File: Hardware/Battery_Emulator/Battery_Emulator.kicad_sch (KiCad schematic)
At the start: 15 parts, among them J1 Screw_Terminal_01x02, J2 USB4105-GF-A-060, U10 ATmega328PB-A, U3 74AHC2G125DP,125, U4 FT230XS-R, U5 LM7805_TO220, U9 ECS-160-7-33B2-CTN-TR3

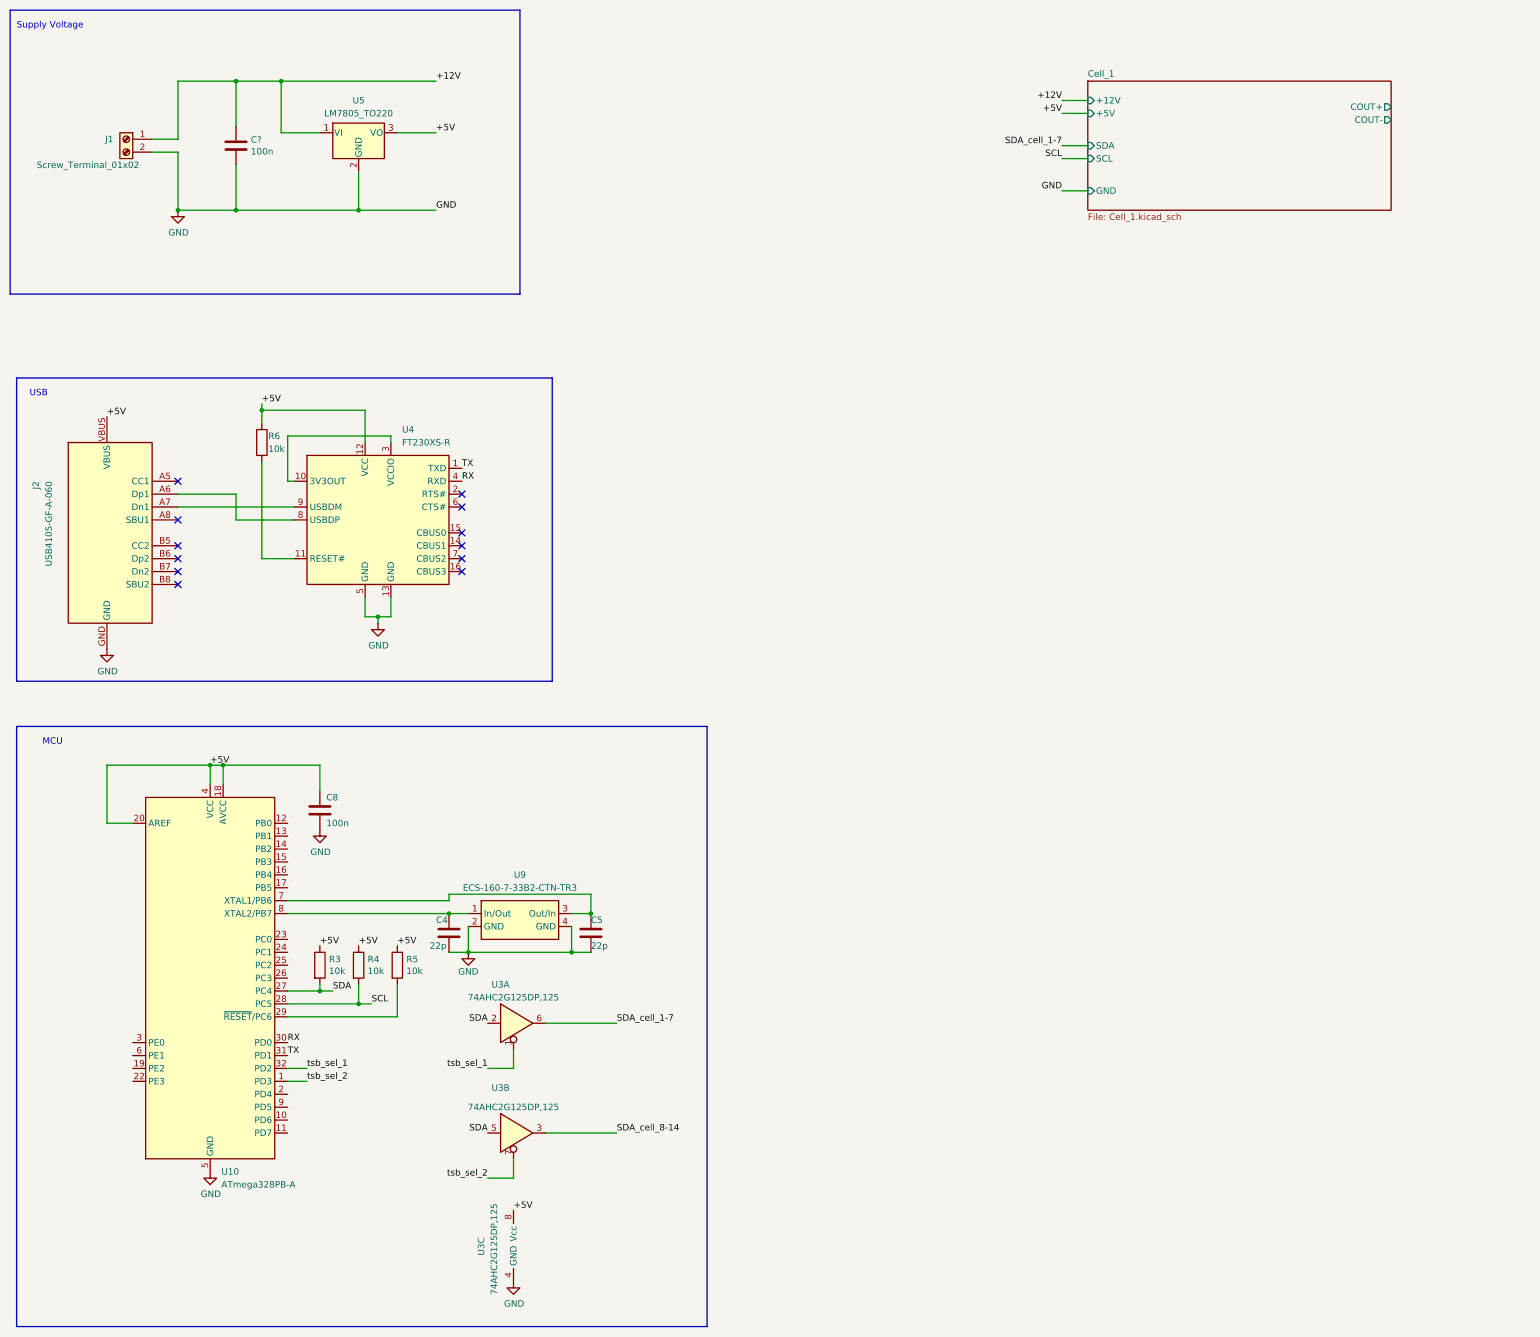
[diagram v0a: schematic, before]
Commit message: Updated schematic battery emulator
Made schematic more clear. Fixed some bugs
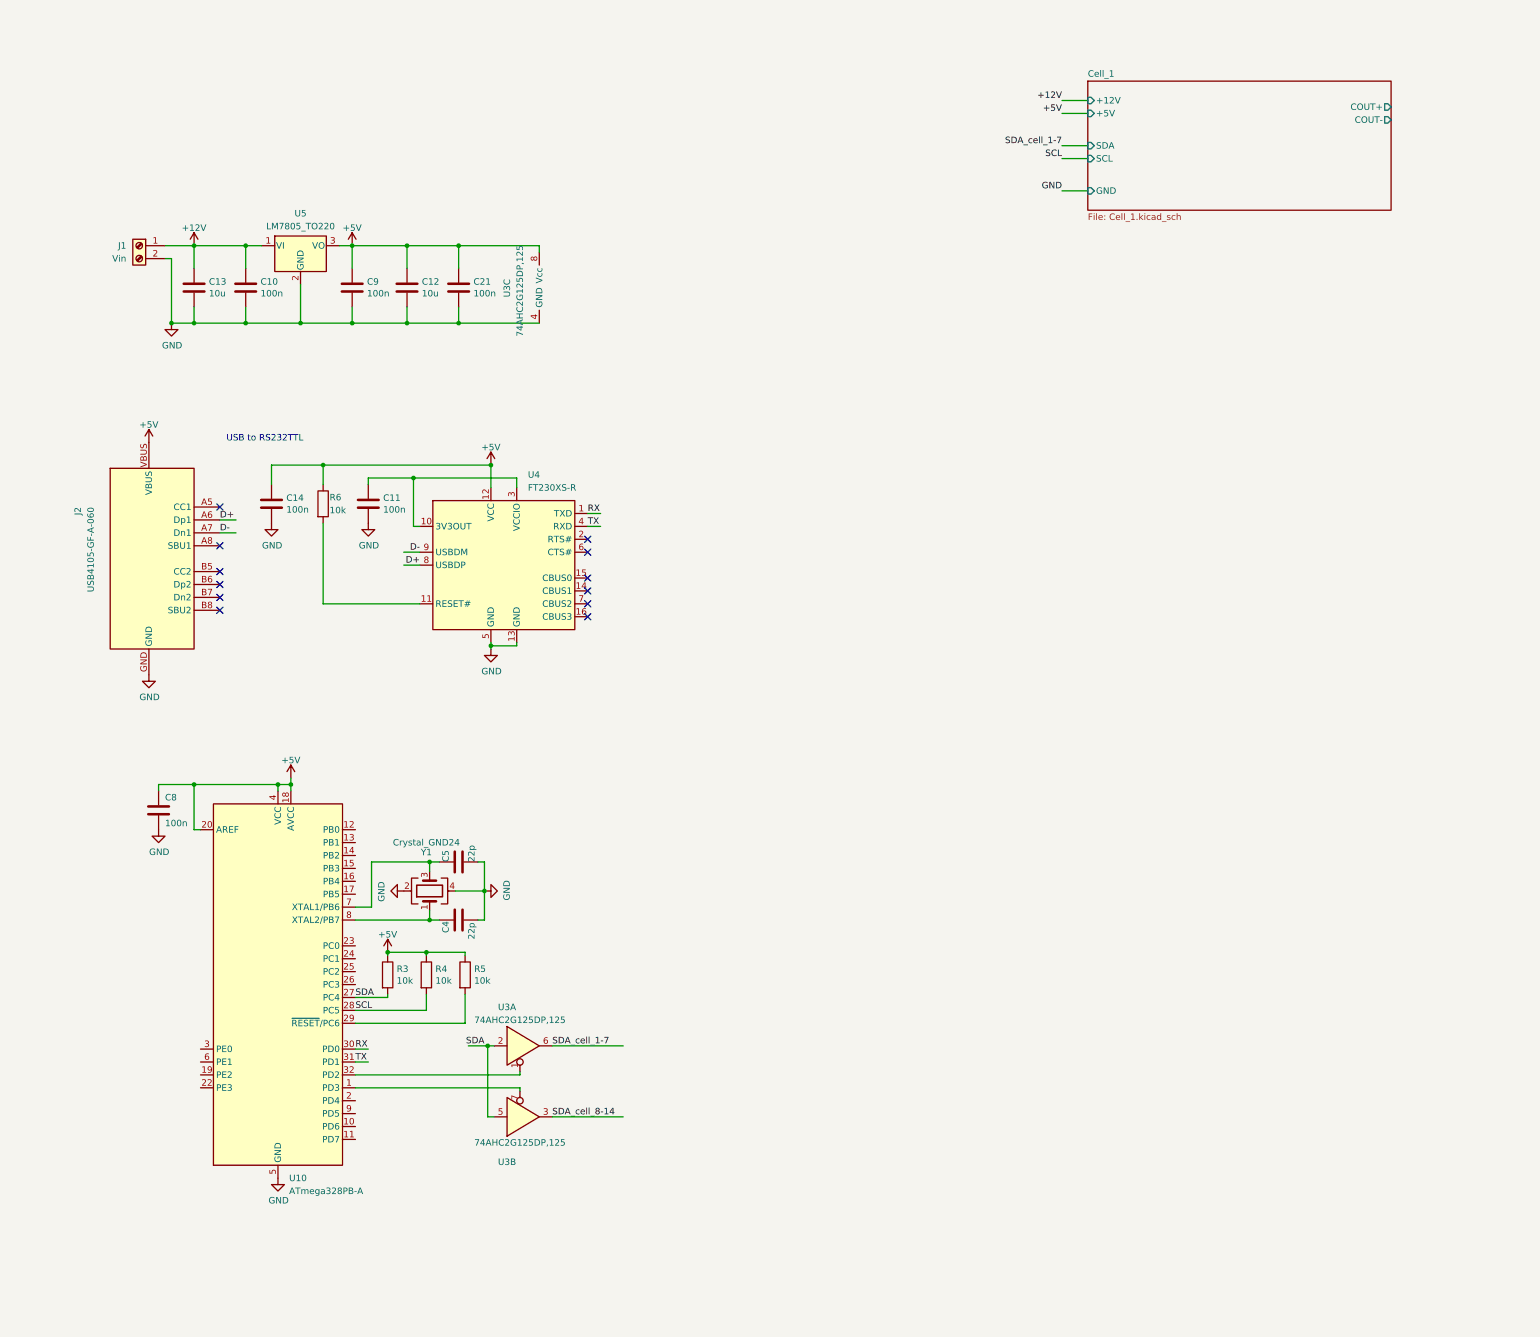
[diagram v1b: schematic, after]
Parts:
- removed U9: ECS-160-7-33B2-CTN-TR3, Crystal:Crystal_SMD_3225-4Pin_3.2x2.5mm, symbol PR7 Custom:ECS-160-7-33B2-CTN-TR3
- added C11, C14, C21, C9: 100n, Capacitor_SMD:C_0805_2012Metric, symbol Device:C
- added C12, C13: 10u, Capacitor_SMD:C_0805_2012Metric, symbol Device:C
- added Y1: Crystal_GND24, Crystal:Crystal_SMD_3225-4Pin_3.2x2.5mm, symbol Device:Crystal_GND24
- J1: value Screw_Terminal_01x02 -> Vin
- gave numbers to parts that had none: 1
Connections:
- net +12V: now also C13.1
- net +5V: now also C12.1, C14.1, C21.1, C9.1
- net GND: now also C11.2, C12.2, C13.2, C14.2, C21.2, C9.2, Y1.2, Y1.4
- net RX: now also U4.1 (TXD); no longer U4.4 (RXD)
- net TX: now also U4.4 (RXD); no longer U4.1 (TXD)
- net D+: now reaches J2.A6 (Dp1), U4.8 (USBDP)
- net D-: now reaches J2.A7 (Dn1), U4.9 (USBDM)
- net at C5.1, U10.7 (XTAL1/PB6): now also Y1.3
- net at C4.1, U10.8 (XTAL2/PB7): now also Y1.1
- net at U4.10 (3V3OUT), U4.3 (VCCIO): now also C11.1
- net tsb_sel_1: no longer names the net of U10.32 (PD2), U3.1
- net tsb_sel_2: no longer names the net of U10.1 (PD3), U3.7
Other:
- note added: "USB to RS232TTL"
- note removed: "MCU"
- note removed: "Supply Voltage"
- note removed: "USB"
- moved on the sheet: C10, C4, C5, C8, J1, J2, R3, R4, R5, R6, U10, U3A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

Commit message: Added components to PCB and started the layout
Also added footprints for the pots, jumpers and power connector
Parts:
- J1: footprint (none) -> Connector_PinSocket_2.00mm:PinSocket_1x02_P2.00mm_Vertical
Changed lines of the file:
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@@
       (effects (font (size 1.27 1.27)) (justify left))
     )
-    (property "Footprint" "" (at 39.37 60.325 0)
+    (property "Footprint" "Connector_PinSocket_2.00mm:PinSocket_1x02_P2.00mm_Vertical" (at 39.37 60.325 0)
       (effects (font (size 1.27 1.27)) hide)
     )

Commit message: Update PCB
Made PCB in Kicad
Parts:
- added C22: 100n, Capacitor_SMD:C_0805_2012Metric, symbol Device:C
- added J3: Cell1_Vout, TerminalBlock_Phoenix:TerminalBlock_Phoenix_MKDS-1,5-2-5.08_1x02_P5.08mm_Horizontal, symbol Connector:Screw_Terminal_01x02
- J1: footprint Connector_PinSocket_2.00mm:PinSocket_1x02_P2.00mm_Vertical -> TerminalBlock_Phoenix:TerminalBlock_Phoenix_MKDS-1,5-2-5.08_1x02_P5.08mm_Horizontal
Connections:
- net +5V: now also C22.1; no longer J2.VBUS
- net Cell_1/COUT+: now also J3.1 (Pin_1)
- net Cell_1/COUT-: now also J3.2 (Pin_2)
- net GND: now also C22.2
- no-connect marks 12 -> 13
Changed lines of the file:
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@@
   (junction (at 45.72 75.565) (diameter 0) (color 0 0 0 0)
+  )
+  (junction (at 43.18 166.37) (diameter 0) (color 0 0 0 0)
   )
   (junction (at 71.12 75.565) (diameter 0) (color 0 0 0 0)
@@
   (no_connect (at 127.635 125.73))
   (no_connect (at 55.245 129.54))
+  (no_connect (at 41.275 99.06))
   (no_connect (at 127.635 118.11))
   (no_connect (at 127.635 120.65))
@@
     (stroke (width 0) (type default))
   )
+  (wire (pts (xy 34.29 167.64) (xy 34.29 166.37))
+    (stroke (width 0) (type default))
+  )
   (wire (pts (xy 113.665 106.045) (xy 113.665 107.95))
     (stroke (width 0) (type default))
@@
     (stroke (width 0) (type default))
   )
+  (wire (pts (xy 285.75 35.56) (xy 292.735 35.56))
+    (stroke (width 0) (type default))
+  )
   (wire (pts (xy 81.915 193.04) (xy 96.52 193.04))
     (stroke (width 0) (type default))
@@
     (stroke (width 0) (type default))
   )
+  (wire (pts (xy 34.29 166.37) (xy 43.18 166.37))
+    (stroke (width 0) (type default))
+  )
   (wire (pts (xy 60.325 75.565) (xy 71.12 75.565))
     (stroke (width 0) (type default))
   )
   (wire (pts (xy 69.215 165.1) (xy 69.215 166.37))
+    (stroke (width 0) (type default))
+  )
+  (wire (pts (xy 285.75 33.02) (xy 292.735 33.02))
     (stroke (width 0) (type default))
   )
@@
       (effects (font (size 1.27 1.27)) (justify left))
     )
-    (property "Footprint" "Connector_PinSocket_2.00mm:PinSocket_1x02_P2.00mm_Vertical" (at 39.37 60.325 0)
+    (property "Footprint" "TerminalBlock_Phoenix:TerminalBlock_Phoenix_MKDS-1,5-2-5.08_1x02_P5.08mm_Horizontal" (at 39.37 60.325 0)
       (effects (font (size 1.27 1.27)) hide)
     )
@@
         (path "/bb7641ff-0dfd-4f4a-b3be-57afbbb9fdac"
           (reference "J1") (unit 1)
+        )
+      )
+    )
+  )
+  (symbol (lib_id "Connector:Screw_Terminal_01x02") (at 297.815 33.02 0) (unit 1)
+    (in_bom yes) (on_board yes) (dnp no)
+    (property "Reference" "J3" (at 300.355 33.02 0)
+      (effects (font (size 1.27 1.27)) (justify left))
+    )
+    (property "Value" "Cell1_Vout" (at 300.355 35.56 0)
+      (effects (font (size 1.27 1.27)) (justify left))
+    )
+    (property "Footprint" "TerminalBlock_Phoenix:TerminalBlock_Phoenix_MKDS-1,5-2-5.08_1x02_P5.08mm_Horizontal" (at 297.815 33.02 0)
+      (effects (font (size 1.27 1.27)) hide)
+    )
+    (property "Datasheet" "~" (at 297.815 33.02 0)
+      (effects (font (size 1.27 1.27)) hide)
+    )
+    (pin "1")
+    (pin "2")
+    (instances
+      (project "Battery_Emulator"
+        (path "/bb7641ff-0dfd-4f4a-b3be-57afbbb9fdac"
+          (reference "J3") (unit 1)
         )
       )
@@
         (path "/bb7641ff-0dfd-4f4a-b3be-57afbbb9fdac/86a0f187-fc20-4f8c-b621-2752c8234446"
           (reference "R1") (unit 1)
+        )
+      )
+    )
+  )
+  (symbol (lib_id "power:GND") (at 34.29 175.26 0) (unit 1)
+    (in_bom yes) (on_board yes) (dnp no)
+    (property "Reference" "#PWR016" (at 34.29 181.61 0)
+      (effects (font (size 1.27 1.27)) hide)
+    )
+    (property "Value" "GND" (at 34.417 179.6542 0)
+      (effects (font (size 1.27 1.27)))
+    )
+    (property "Footprint" "" (at 34.29 175.26 0)
+      (effects (font (size 1.27 1.27)) hide)
+    )
+    (property "Datasheet" "" (at 34.29 175.26 0)
+      (effects (font (size 1.27 1.27)) hide)
+    )
+    (pin "1")
+    (instances
+      (project "Battery_Emulator"
+        (path "/bb7641ff-0dfd-4f4a-b3be-57afbbb9fdac"
+          (reference "#PWR016") (unit 1)
         )
       )
@@
     )
   )
-  (symbol (lib_id "power:+5V") (at 41.275 99.06 0) (unit 1)
-    (in_bom yes) (on_board yes) (dnp no) (fields_autoplaced)
-    (property "Reference" "#PWR010" (at 41.275 102.87 0)
-      (effects (font (size 1.27 1.27)) hide)
-    )
-    (property "Value" "+5V" (at 41.275 95.5581 0)
-      (effects (font (size 1.27 1.27)))
-    )
-    (property "Footprint" "" (at 41.275 99.06 0)
-      (effects (font (size 1.27 1.27)) hide)
-    )
-    (property "Datasheet" "" (at 41.275 99.06 0)
-      (effects (font (size 1.27 1.27)) hide)
-    )
-    (pin "1")
-    (instances
-      (project "Battery_Emulator"
-        (path "/bb7641ff-0dfd-4f4a-b3be-57afbbb9fdac"
-          (reference "#PWR010") (unit 1)
-        )
-      )
-    )
-  )
   (symbol (lib_id "Device:Crystal_GND24") (at 96.52 187.325 90) (unit 1)
     (in_bom yes) (on_board yes) (dnp no)
@@
         )
       )
+    )
+  )
+  (symbol (lib_id "Device:C") (at 34.29 171.45 0) (unit 1)
+    (in_bom yes) (on_board yes) (dnp no)
+    (property "Reference" "C22" (at 35.56 168.91 0)
+      (effects (font (size 1.27 1.27)) (justify left))
+    )
+    (property "Value" "100n" (at 35.56 173.99 0)
+      (effects (font (size 1.27 1.27)) (justify left))
+    )
+    (property "Footprint" "Capacitor_SMD:C_0805_2012Metric" (at 35.2552 175.26 0)
+      (effects (font (size 1.27 1.27)) hide)
+    )
+    (property "Datasheet" "~" (at 34.29 171.45 0)
+      (effects (font (size 1.27 1.27)) hide)
+    )
+    (pin "1")
+    (pin "2")
+    (instances
+      (project "Battery_Emulator"
+        (path "/bb7641ff-0dfd-4f4a-b3be-57afbbb9fdac"
+          (reference "C22") (unit 1)
+        )
+      )

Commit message: Update PCB design
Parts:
- removed U5: LM7805_TO220, Package_TO_SOT_THT:TO-220-3_Vertical, symbol Regulator_Linear:LM7805_TO220
- added U9: KA78M05_TO252, Package_TO_SOT_SMD:TO-252-2, symbol Regulator_Linear:KA78M05_TO252
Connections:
- net +12V: now also U9.1 (VI)
- net +5V: now also U9.3 (VO)
- net GND: now also U9.2 (GND)
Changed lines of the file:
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@@
+    (stroke (width 0) (type default))
+  )
+  (wire (pts (xy 71.12 67.945) (xy 71.12 75.565))
     (stroke (width 0) (type default))
   )
@@
   )
   (wire (pts (xy 81.915 208.28) (xy 88.265 208.28))
-    (stroke (width 0) (type default))
-  )
-  (wire (pts (xy 71.12 67.945) (xy 71.12 75.565))
     (stroke (width 0) (type default))
   )
@@
     )
   )
-  (symbol (lib_id "Regulator_Linear:LM7805_TO220") (at 71.12 60.325 0) (unit 1)
-    (in_bom yes) (on_board yes) (dnp no) (fields_autoplaced)
-    (property "Reference" "U5" (at 71.12 53.975 0)
-      (effects (font (size 1.27 1.27)))
-    )
-    (property "Value" "LM7805_TO220" (at 71.12 56.515 0)
-      (effects (font (size 1.27 1.27)))
-    )
-    (property "Footprint" "Package_TO_SOT_THT:TO-220-3_Vertical" (at 71.12 54.61 0)
-      (effects (font (size 1.27 1.27) italic) hide)
-    )
-    (property "Datasheet" "https://www.onsemi.cn/PowerSolutions/document/MC7800-D.PDF" (at 71.12 61.595 0)
-      (effects (font (size 1.27 1.27)) hide)
-    )
-    (pin "1")
-    (pin "2")
-    (pin "3")
-    (instances
-      (project "Battery_Emulator"
-        (path "/bb7641ff-0dfd-4f4a-b3be-57afbbb9fdac"
-          (reference "U5") (unit 1)
-        )
-      )
-    )
-  )
   (symbol (lib_id "Device:C") (at 102.235 68.58 0) (unit 1)
     (in_bom yes) (on_board yes) (dnp no)
@@
         )
       )
+    )
+  )
+  (symbol (lib_id "Regulator_Linear:KA78M05_TO252") (at 71.12 60.325 0) (unit 1)
+    (in_bom yes) (on_board yes) (dnp no) (fields_autoplaced)
+    (property "Reference" "U9" (at 71.12 55.4101 0)
+      (effects (font (size 1.27 1.27)))
+    )
+    (property "Value" "KA78M05_TO252" (at 71.12 57.3311 0)
+      (effects (font (size 1.27 1.27)))
+    )
+    (property "Footprint" "Package_TO_SOT_SMD:TO-252-2" (at 71.12 54.61 0)
+      (effects (font (size 1.27 1.27) italic) hide)
+    )
+    (property "Datasheet" "https://www.onsemi.com/pub/Collateral/MC78M00-D.PDF" (at 71.12 61.595 0)
+      (effects (font (size 1.27 1.27)) hide)
+    )
+    (pin "1")
+    (pin "2")
+    (pin "3")
+    (instances
+      (project "Battery_Emulator"
+        (path "/bb7641ff-0dfd-4f4a-b3be-57afbbb9fdac"
+          (reference "U9") (unit 1)
+        )
+      )
